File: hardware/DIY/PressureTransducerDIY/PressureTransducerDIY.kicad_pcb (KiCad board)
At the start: 2 copper layers, 66 x 48.3 mm, 11 parts, among them J1 JST_Power_Connector_Female, J2 PinHeader_Female_MS5803, U1 ATmega328P-PU, U2 MCP1700-3302E_TO92

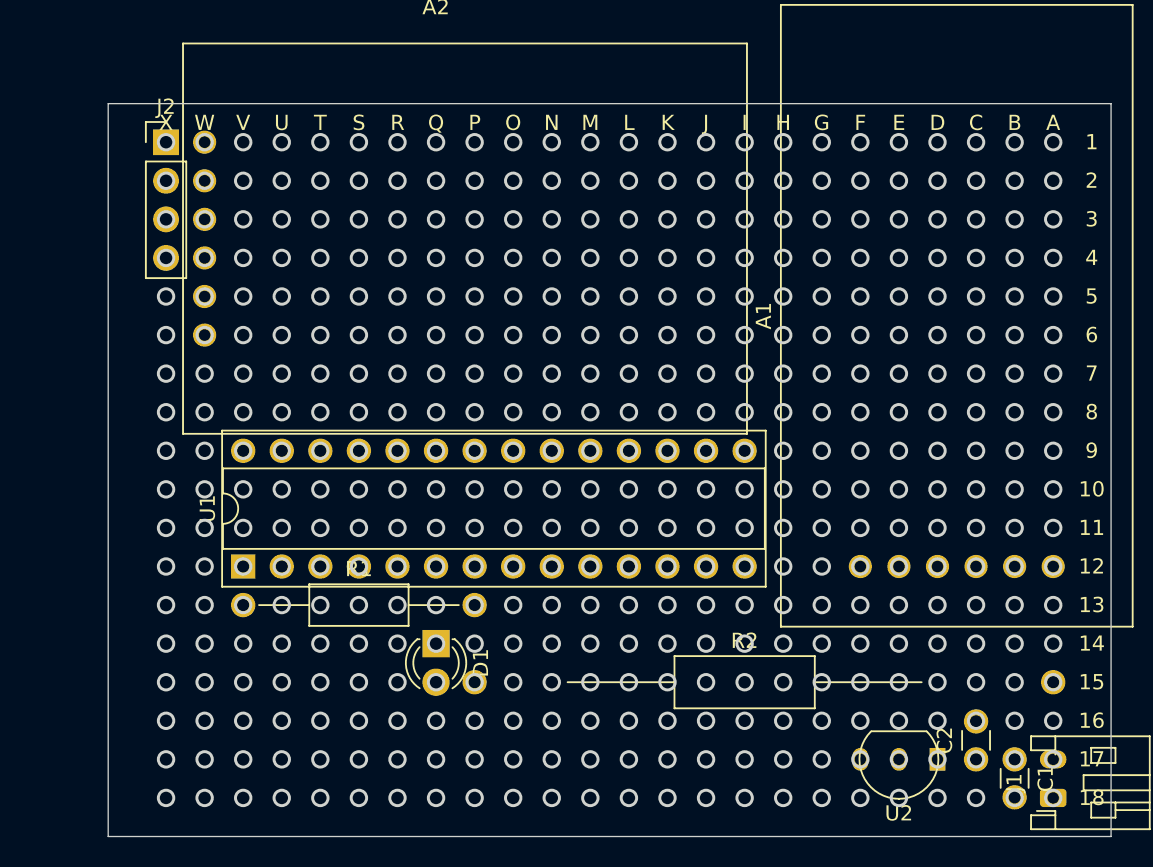
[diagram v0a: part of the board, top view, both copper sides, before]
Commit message: Add serial pin header and swap sensor header to JST type
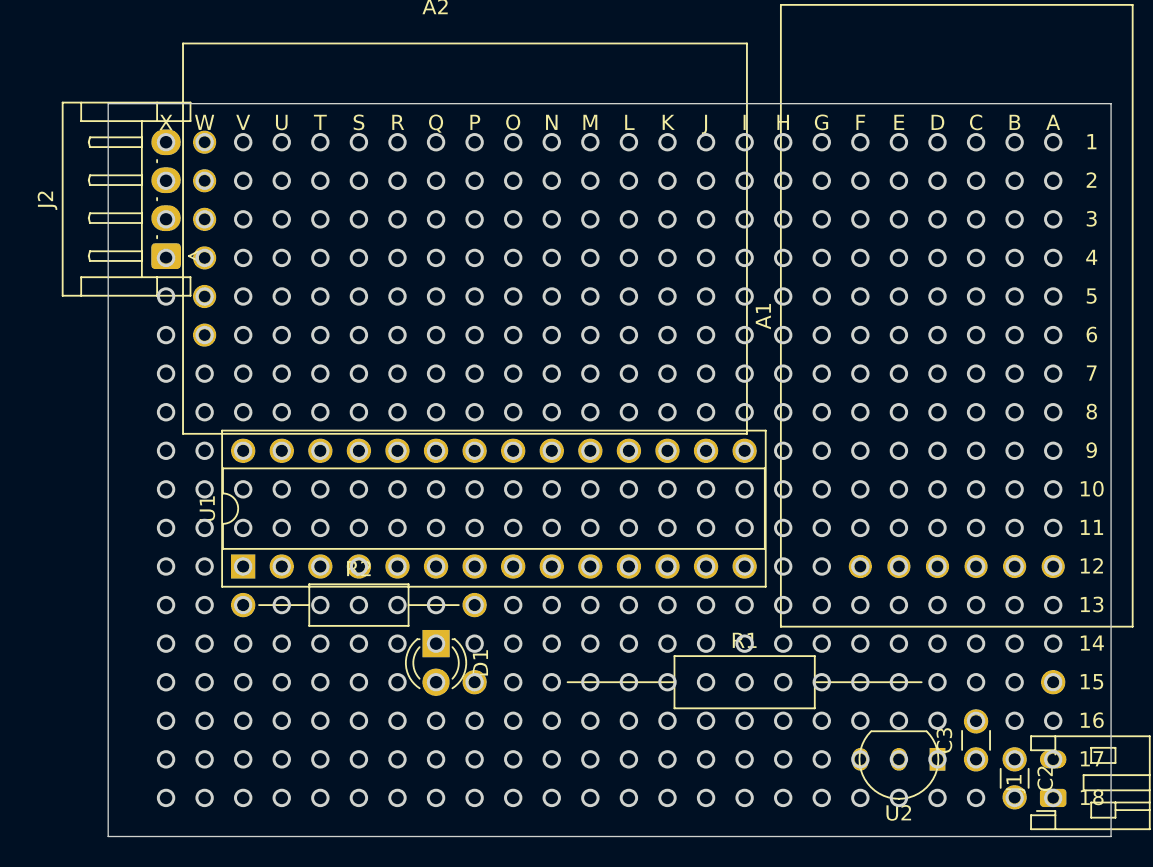
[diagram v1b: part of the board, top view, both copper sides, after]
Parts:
- J2: footprint Connector_PinHeader_2.54mm:PinHeader_1x04_P2.54mm_Vertical -> Connector_JST:JST_EH_S4B-EH_1x04_P2.50mm_Horizontal
- moved J2 7.50 mm to (142.2, 98.9), turned to 90 degrees
- renumbered C1 to C2, C2 to C3, R2 to R1, R1 to R2
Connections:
- net Net-(U1-Pad2) renamed TX
- D1 pad 1: GND -> Net-(D1-Pad1)
- R1 pad 1: Net-(D1-Pad2) -> GND
- R1 pad 2: Net-(R2-Pad2) -> Net-(D1-Pad1)
- U1 pad 3: Alarm1 -> RX
- U1 pad 4: Net-(U1-Pad4) -> Alarm1
- U1 pad 6: Net-(R2-Pad2) -> Net-(D1-Pad2)

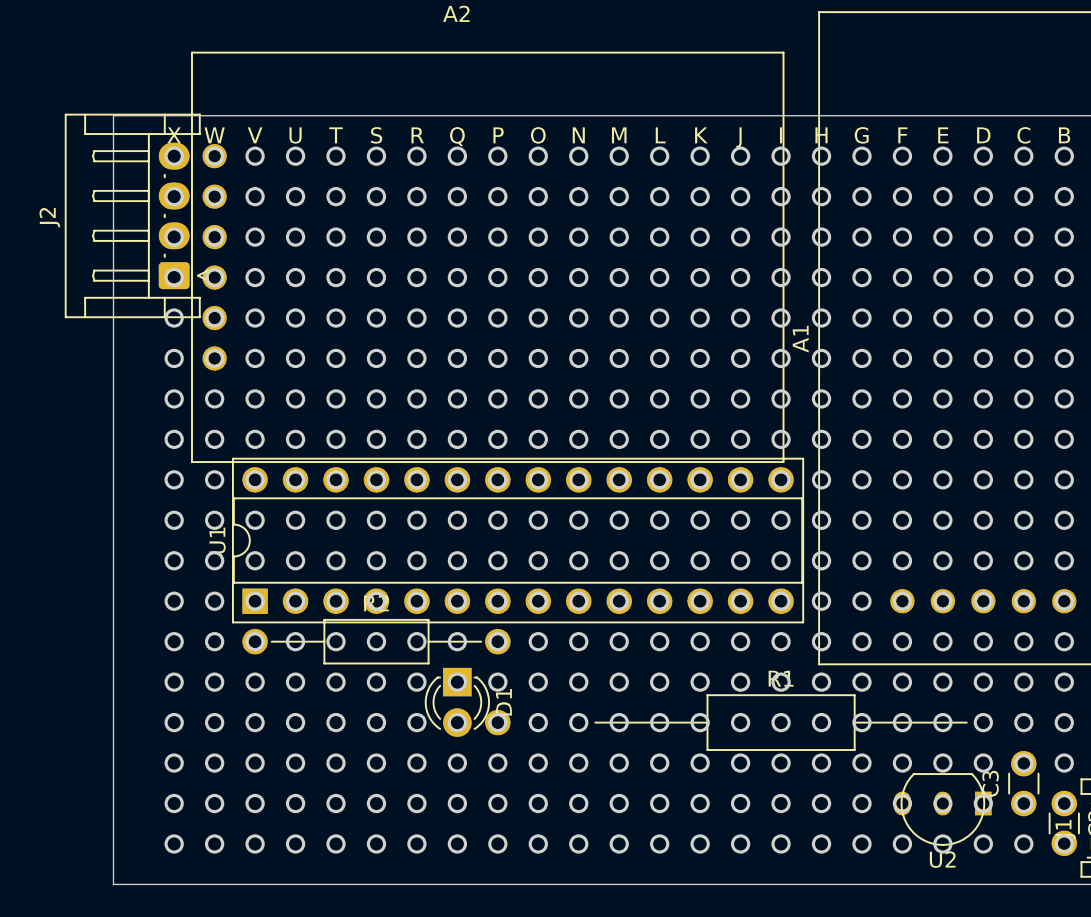
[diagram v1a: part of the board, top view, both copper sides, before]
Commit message: Change 4 pin JST to female header, add 3 female pins for Serial programmign
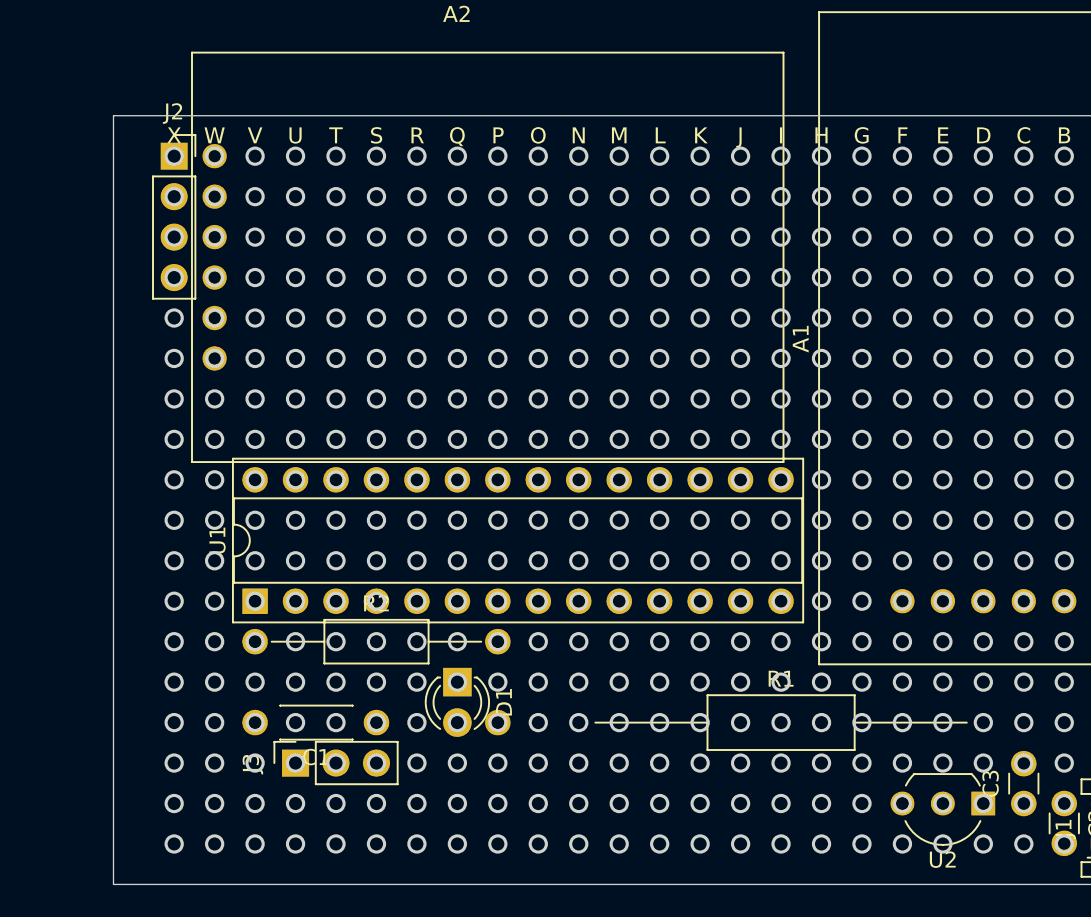
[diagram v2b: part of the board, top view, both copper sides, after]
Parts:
- added C1: 0.1uF, Capacitor_THT:C_Disc_D4.3mm_W1.9mm_P5.00mm, F.Cu at (153.7, 127.0)
- added J3: PinHeader_Female_Serial, Connector_PinSocket_2.54mm:PinSocket_1x03_P2.54mm_Vertical, F.Cu at (149.9, 129.5)
- J2: footprint Connector_JST:JST_EH_S4B-EH_1x04_P2.50mm_Horizontal -> Connector_PinSocket_2.54mm:PinSocket_1x04_P2.54mm_Vertical
- U2: value MCP1700-3302E_TO92 -> MCP1700-3002E_TO92; footprint Package_TO_SOT_THT:TO-92_Inline -> Package_TO_SOT_THT:TO-92_Inline_Wide
- moved J2 7.50 mm to (142.2, 91.4), turned to 0 degrees
- moved U2 1.27 mm to (193.0, 132.1)

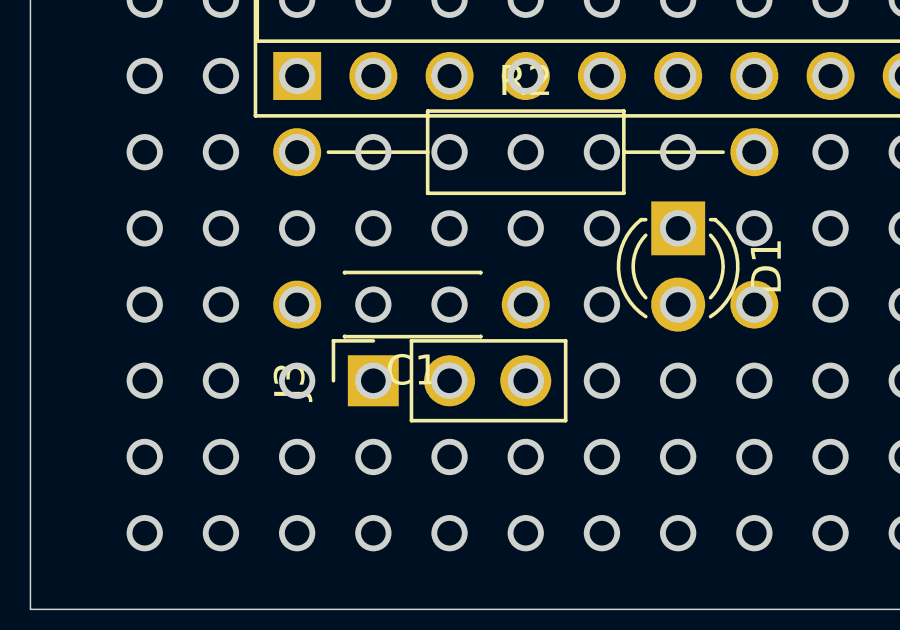
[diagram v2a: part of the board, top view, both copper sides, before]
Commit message: Fix wiring issue with VREG VCC going to GND
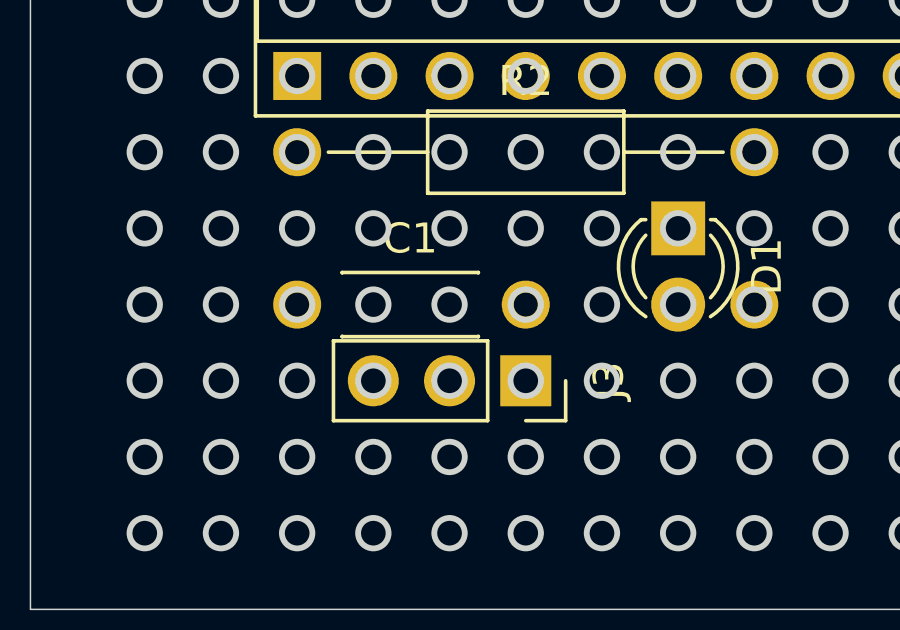
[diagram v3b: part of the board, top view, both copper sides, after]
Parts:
- moved C1 5.08 mm to (148.6, 127.0), turned to 0 degrees
- moved J3 5.08 mm to (154.9, 129.5), turned to 270 degrees

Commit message: Restart for new set of assembly photos
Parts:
- removed J1: JST_Power_Connector_Female, Connector_JST:JST_PH_S2B-PH-K_1x02_P2.00mm_Horizontal
- moved A2 85.2 mm to (245.1, 102.9)
- moved C1 85.2 mm to (233.7, 132.1)
- moved C3 85.2 mm to (280.7, 137.2)
- moved D1 85.2 mm to (245.1, 129.5)
- moved J2 85.2 mm to (227.3, 96.5)
- moved J3 85.2 mm to (240.0, 134.6)
- moved R1 85.2 mm to (252.7, 132.1)
- moved R2 85.2 mm to (232.4, 127.0)
- moved U2 85.2 mm to (278.1, 137.2)
- moved C2 85.2 mm to (283.2, 137.2)

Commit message: Finished new assembly photos
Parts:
- added J1: JST_Power_Connector_Female, Connector_JST:JST_PH_B2B-PH-K_1x02_P2.00mm_Vertical, F.Cu at (200.7, 134.6)
- moved C3 87.8 mm to (193.0, 132.1)
- moved U2 87.8 mm to (190.5, 132.1)
- moved C2 87.8 mm to (195.6, 132.1)
- moved A2 85.2 mm to (160.0, 97.8)
- moved C1 85.2 mm to (148.6, 127.0)
- moved D1 85.2 mm to (160.0, 124.5)
- moved J2 85.2 mm to (142.2, 91.4)
- moved J3 85.2 mm to (154.9, 129.5)
- moved R2 85.2 mm to (147.3, 121.9)
- moved R1 84.0 mm to (168.9, 127.0)
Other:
- outline, holes or cut-outs redrawn
